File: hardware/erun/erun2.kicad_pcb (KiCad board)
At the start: 2 copper layers, 73.7 x 92.1 mm, 25 parts, among them J1 Conn_Coaxial, J10 Conn_01x03_Female, J2 HEIDENHAIN_MT25_TTL, J3 TRIGGER_TTL, J4 Conn_01x02_Female, J5 Conn_01x02_Female, J6 Conn_01x02_Female, J7 Conn_01x02_Female, J8 Conn_01x02_Female, J9 Conn_01x03_Female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

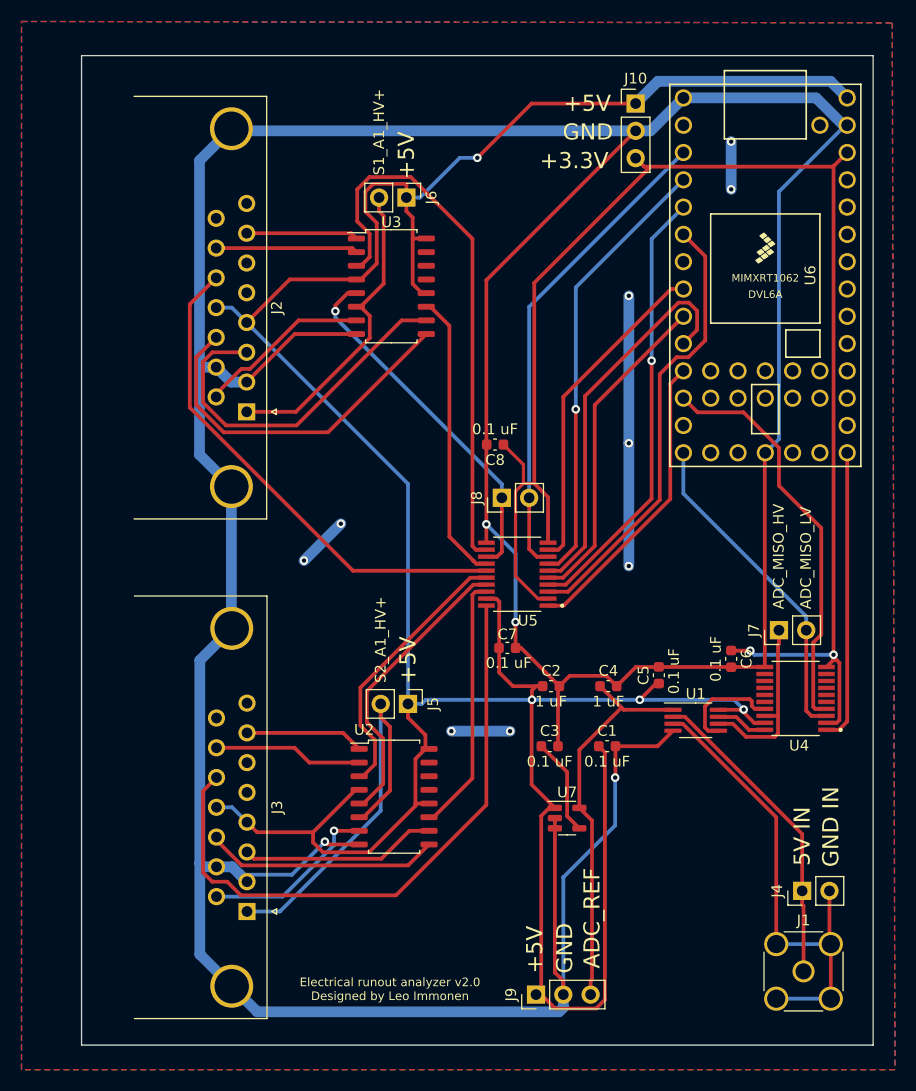
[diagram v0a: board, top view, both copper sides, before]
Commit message: Added low pass filter and minor refinements
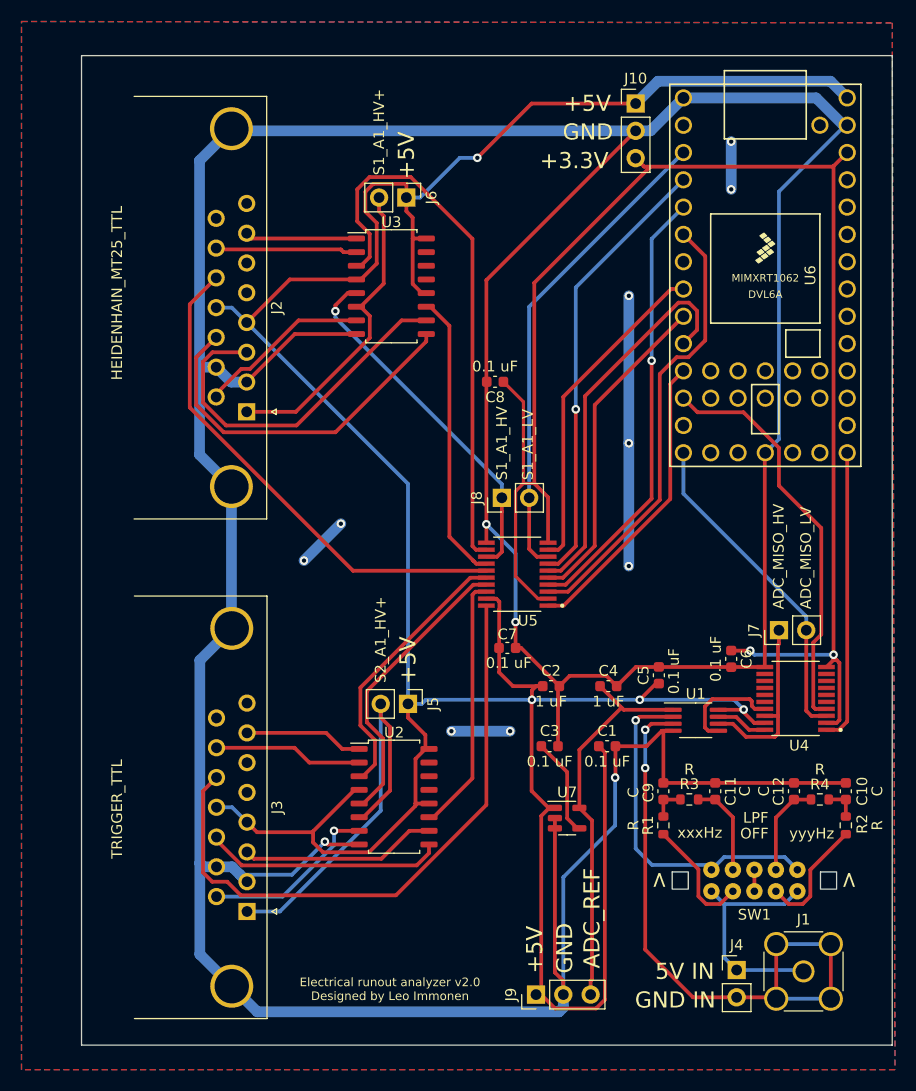
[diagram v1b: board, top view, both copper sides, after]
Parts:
- added C10: C, Capacitor_SMD:C_0603_1608Metric, F.Cu at (81.2, 78.5)
- added C11: C, Capacitor_SMD:C_0603_1608Metric, F.Cu at (69.0, 78.5)
- added C12: C, Capacitor_SMD:C_0603_1608Metric, F.Cu at (76.3, 78.5)
- added C9: C, Capacitor_SMD:C_0603_1608Metric, F.Cu at (64.2, 78.5)
- added R1: R, Resistor_SMD:R_0603_1608Metric, F.Cu at (64.2, 81.7)
- added R2: R, Resistor_SMD:R_0603_1608Metric, F.Cu at (81.2, 81.7)
- added R3: R, Resistor_SMD:R_0603_1608Metric, F.Cu at (66.6, 79.2)
- added R4: R, Resistor_SMD:R_0603_1608Metric, F.Cu at (78.7, 79.2)
- added SW1: SW_DP3T, SW_DP3T:SW_DP3T, F.Cu at (72.6, 86.8)
- moved J4 9.56 mm to (71.0, 95.1), turned to 0 degrees
- moved C8 5.84 mm to (48.5, 40.4)
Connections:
- net /ADC_INGND renamed /ANALOG_GND
- J1 pad 1: /ADC_IN5V -> /ANALOG_5V
- J4 pad 1: /ADC_IN5V -> /ANALOG_5V
- U1 pad 2: /ADC_IN5V -> /ANALOG_5V_LPF
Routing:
- net /ANALOG_5V_LPF: track 0.00 -> 32.4 mm, vias 0 -> 1
- net /ADC_IN5V: track 29.4 -> 0.00 mm
- net /ANALOG_5V: track 0.00 -> 22.3 mm
- net GND: track 442.1 -> 464.0 mm
- net /ANALOG_GND: track 45.3 -> 57.9 mm, vias 0 -> 2
- net Net-(R2-Pad1): track 0.00 -> 11.1 mm
- net Net-(R1-Pad1): track 0.00 -> 11.1 mm
- net Net-(C11-Pad2): track 0.00 -> 9.88 mm
- net Net-(C12-Pad1): track 0.00 -> 8.82 mm
- net +3V3: track 142.7 -> 148.5 mm
- net Net-(C10-Pad1): track 0.00 -> 3.17 mm
- net Net-(C9-Pad2): track 0.00 -> 3.15 mm
- net Net-(SW1-Pad2): track 0.00 -> 2.00 mm
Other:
- board size 73.7 x 92.1 mm -> 75.4 x 92.1 mm
- board text added: ">"
- board text added: "LPF"
- board text added: "OFF"
- board text added: "S1_A1_HV"
- board text added: "S1_A1_LV"
- board text added: "xxxHz"
- board text added: "yyyHz"

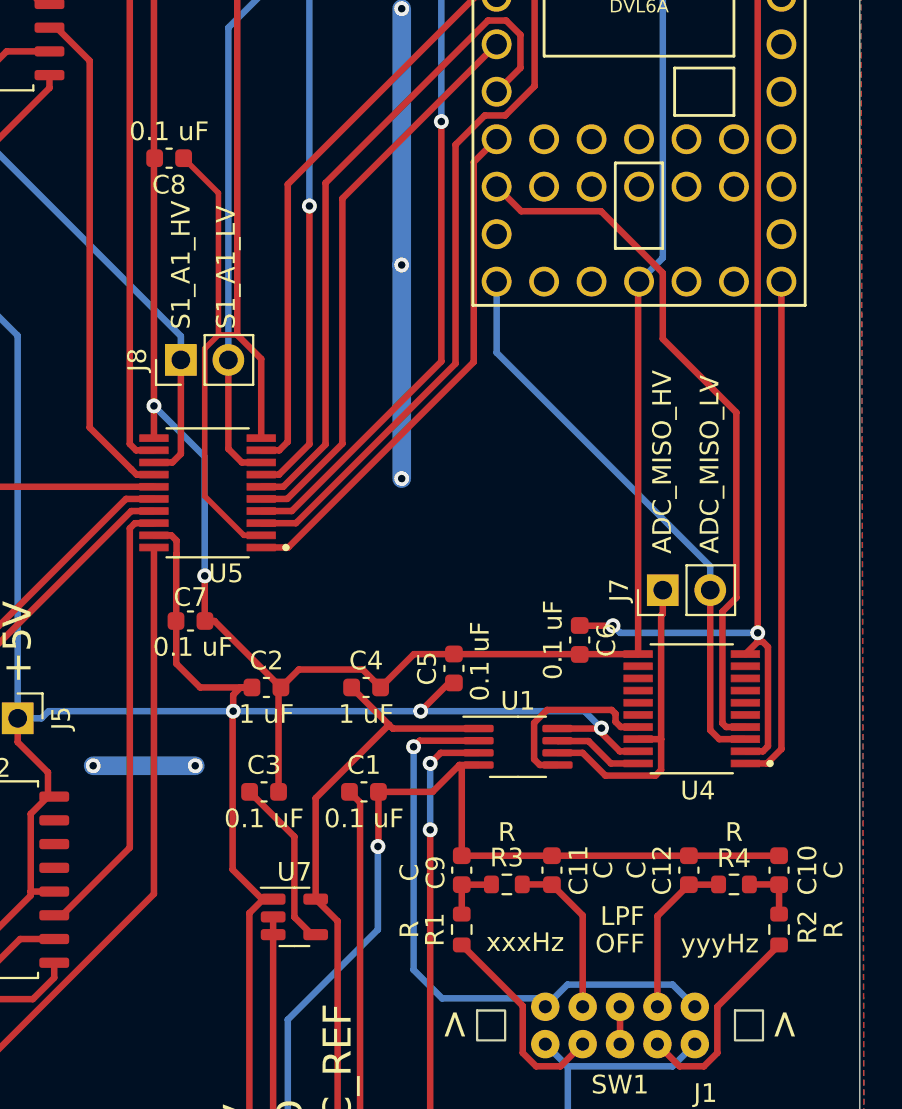
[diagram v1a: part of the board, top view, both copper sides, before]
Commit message: Updated some labels
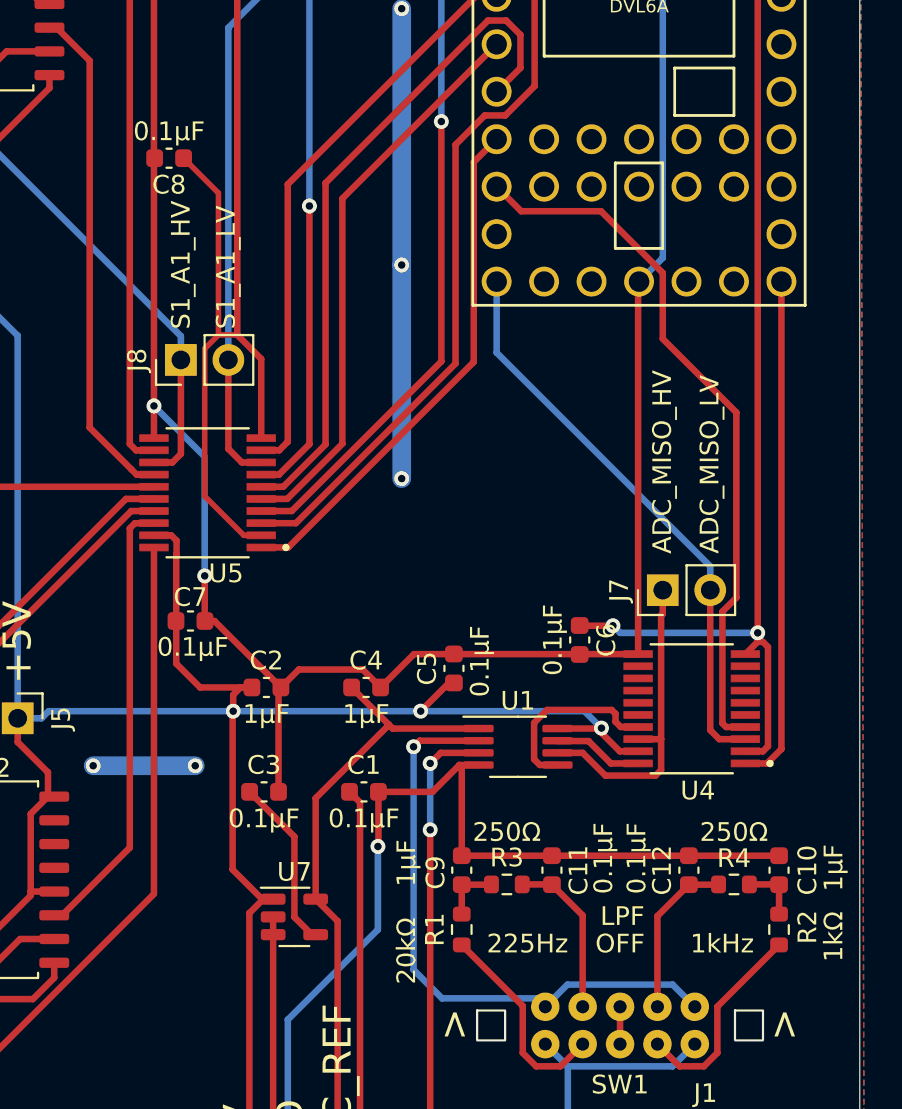
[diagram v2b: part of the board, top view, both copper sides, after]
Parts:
- C1, C3, C5, C6, C7, C8: value 0.1 uF -> 0.1μF
- C10, C9: value C -> 1μF
- C11, C12: value C -> 0.1μF
- C2, C4: value 1 uF -> 1μF
- R1: value R -> 20kΩ
- R2: value R -> 1kΩ
- R3, R4: value R -> 250Ω
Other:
- board text added: "1kHz"
- board text added: "225Hz"
- board text removed: "xxxHz"
- board text removed: "yyyHz"
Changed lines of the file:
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@@
       (effects (font (size 1 1) (thickness 0.15)))
     )
-    (fp_text value "C" (at 0 -2.7555 90) (layer "F.SilkS")
+    (fp_text value "0.1μF" (at -0.635 -2.7555 90) (layer "F.SilkS")
       (effects (font (size 1 1) (thickness 0.15)))
     )
@@
       (effects (font (size 1 1) (thickness 0.15)))
     )
-    (fp_text value "R" (at 0 -2.794) (layer "F.SilkS")
+    (fp_text value "250Ω" (at 0 -2.794) (layer "F.SilkS")
       (effects (font (size 1 1) (thickness 0.15)))
     )
@@
       (effects (font (size 1 1) (thickness 0.15)))
     )
-    (fp_text value "0.1 uF" (at 0.381 1.397 270) (layer "F.SilkS")
+    (fp_text value "0.1μF" (at 0.381 1.397 270) (layer "F.SilkS")
       (effects (font (size 1 1) (thickness 0.15)))
     )
@@
       (effects (font (size 1 1) (thickness 0.15)))
     )
-    (fp_text value "0.1 uF" (at 0.127 1.397) (layer "F.SilkS")
+    (fp_text value "0.1μF" (at 0.127 1.397) (layer "F.SilkS")
       (effects (font (size 1 1) (thickness 0.15)))
     )
@@
       (effects (font (size 1 1) (thickness 0.15)))
     )
-    (fp_text value "1 uF" (at 0 1.43) (layer "F.SilkS")
+    (fp_text value "1μF" (at 0 1.43) (layer "F.SilkS")
       (effects (font (size 1 1) (thickness 0.15)))
     )
@@
       (effects (font (size 1 1) (thickness 0.15)))
     )
-    (fp_text value "C" (at 0 -2.794 90) (layer "F.SilkS")
+    (fp_text value "0.1μF" (at 0.635 -2.794 90) (layer "F.SilkS")
       (effects (font (size 1 1) (thickness 0.15)))
     )
@@
       (effects (font (size 1 1) (thickness 0.15)))
     )
-    (fp_text value "0.1 uF" (at 0 1.43) (layer "F.SilkS")
+    (fp_text value "0.1μF" (at 0 1.43) (layer "F.SilkS")
       (effects (font (size 1 1) (thickness 0.15)))
     )
@@
       (effects (font (size 1 1) (thickness 0.15)))
     )
-    (fp_text value "0.1 uF" (at 0 1.43 90) (layer "F.SilkS")
+    (fp_text value "0.1μF" (at 0 1.43 90) (layer "F.SilkS")
       (effects (font (size 1 1) (thickness 0.15)))
     )
@@
       (effects (font (size 1 1) (thickness 0.15)))
     )
-    (fp_text value "0.1 uF" (at 0 1.43) (layer "F.SilkS")
+    (fp_text value "0.1μF" (at 0 1.43) (layer "F.SilkS")
       (effects (font (size 1 1) (thickness 0.15)))
     )
@@
       (effects (font (size 1 1) (thickness 0.15)))
     )
-    (fp_text value "1 uF" (at 0 1.43) (layer "F.SilkS")
+    (fp_text value "1μF" (at 0 1.43) (layer "F.SilkS")
       (effects (font (size 1 1) (thickness 0.15)))
     )
@@
       (effects (font (size 1 1) (thickness 0.15)))
     )
-    (fp_text value "R" (at 0 -2.794 90) (layer "F.SilkS")
+    (fp_text value "20kΩ" (at -1.143 -2.9595 90) (layer "F.SilkS")
       (effects (font (size 1 1) (thickness 0.15)))
     )
@@
       (effects (font (size 1 1) (thickness 0.15)))
     )
-    (fp_text value "C" (at 0.127 2.794 90) (layer "F.SilkS")
+    (fp_text value "1μF" (at -0.381 2.9595 90) (layer "F.SilkS")
       (effects (font (size 1 1) (thickness 0.15)))
     )
@@
       (effects (font (size 1 1) (thickness 0.15)))
     )
-    (fp_text value "0.1 uF" (at 0 1.43) (layer "F.SilkS")
+    (fp_text value "0.1μF" (at 0 1.43) (layer "F.SilkS")
       (effects (font (size 1 1) (thickness 0.15)))
     )
@@
       (effects (font (size 1 1) (thickness 0.15)))
     )
-    (fp_text value "C" (at 0 2.921 90) (layer "F.SilkS")
+    (fp_text value "1μF" (at 0.127 2.921 90) (layer "F.SilkS")
       (effects (font (size 1 1) (thickness 0.15)))
     )
@@
       (effects (font (size 1 1) (thickness 0.15)))
     )
-    (fp_text value "R" (at 0 2.921 90) (layer "F.SilkS")
+    (fp_text value "1kΩ" (at -0.381 2.921 90) (layer "F.SilkS")
       (effects (font (size 1 1) (thickness 0.15)))
     )
@@
       (effects (font (size 1 1) (thickness 0.15)))
     )
-    (fp_text value "R" (at 0 2.794) (layer "F.SilkS")
+    (fp_text value "250Ω" (at 0 2.794) (layer "F.SilkS")
       (effects (font (size 1 1) (thickness 0.15)))
     )
@@
     (effects (font (size 1 1) (thickness 0.15)))
   )
-  (gr_text "yyyHz" (at 77.978 82.423) (layer "F.SilkS")
+  (gr_text "1kHz" (at 78.105 82.423) (layer "F.SilkS")
     (effects (font (size 1 1) (thickness 0.15)))
   )
@@
     (effects (font (size 1 1) (thickness 0.25)))
   )
-  (gr_text "xxxHz" (at 67.564 82.349019) (layer "F.SilkS")
+  (gr_text "225Hz" (at 67.691 82.423) (layer "F.SilkS")
     (effects (font (size 1 1) (thickness 0.15)))
   )
